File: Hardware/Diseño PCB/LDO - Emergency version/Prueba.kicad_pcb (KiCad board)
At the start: 2 copper layers, 99.4 x 209.5 mm, 132 parts, among them Q1 BC547, Q10 BC547, Q11 BC557, Q12 BC547, Q13 BC557, Q14 BC547, Q15 BC557, Q16 BC547, Q17 BC547, Q18 BC557, Q19 IRF4905, Q2 BC547, Q3 BC557, Q39 BC547, Q4 BC547, Q40 BC547, Q41 BC557, Q42 BC547, Q43 BC557, Q44 BC547, Q45 BC547, Q46 BC547, Q47 BC557, Q48 BC547, Q49 BC557, Q5 BC557, Q50 BC547, Q51 BC557, Q52 BC547, Q53 BC557, Q54 BC547, Q55 BC547, Q56 BC557, Q57 IRF4905, Q6 BC547, Q7 BC547, Q8 BC547, Q9 BC557, U1 LM324, U2 TL431LP, U5 LM324, U6 TL431LP

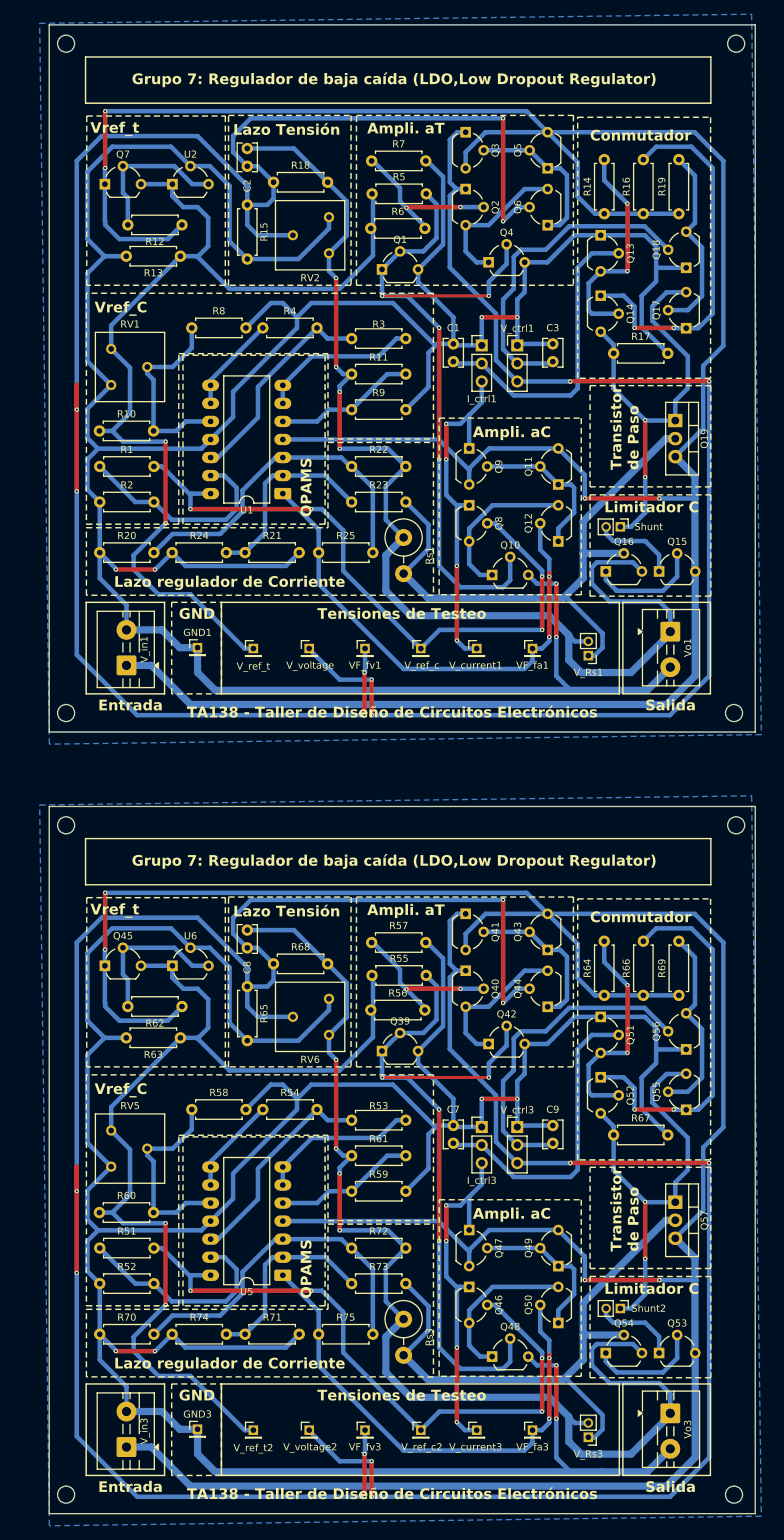
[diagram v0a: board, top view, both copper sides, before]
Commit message: Correcciones menores en emergency version
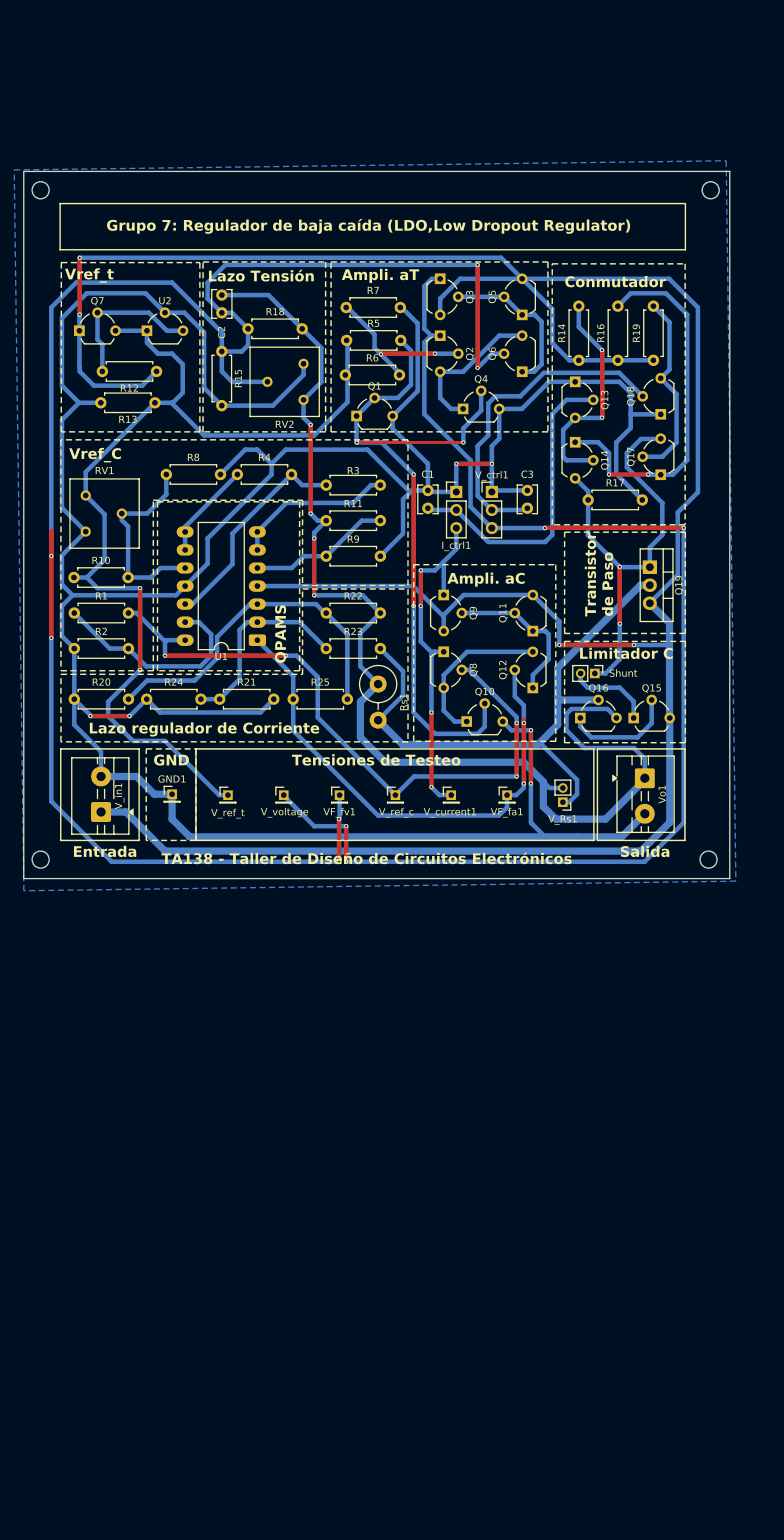
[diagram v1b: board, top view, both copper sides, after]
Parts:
- removed C7: 220 nF, Capacitor_THT:C_Disc_D3.8mm_W2.6mm_P2.50mm
- removed C8: 100pF, Capacitor_THT:C_Disc_D3.8mm_W2.6mm_P2.50mm
- removed C9: 2.2nF, Capacitor_THT:C_Disc_D3.8mm_W2.6mm_P2.50mm
- removed G***2: LOGO, LOGO
- removed GND3: Pin_GND, Connector_PinHeader_2.00mm:PinHeader_1x01_P2.00mm_Vertical
- removed I_ctrl3: I_ctrl, Connector_PinHeader_2.54mm:PinHeader_1x03_P2.54mm_Vertical
- removed Q39, Q40, Q42, Q44, Q45, Q46, Q48, Q50, Q52, Q54, Q55: BC547, Package_TO_SOT_THT:TO-92_Wide
- removed Q41, Q43, Q47, Q49, Q51, Q53, Q56: BC557, Package_TO_SOT_THT:TO-92_Wide
- removed Q57: IRF4905, Package_TO_SOT_THT:TO-220-3_Vertical
- removed R51, R52, R53, R54, R55, R59, R65, R66, R72, R73: 1k, Resistor_THT:R_Axial_DIN0207_L6.3mm_D2.5mm_P7.62mm_Horizontal
- removed R56, R57, R62: 2.2k, Resistor_THT:R_Axial_DIN0207_L6.3mm_D2.5mm_P7.62mm_Horizontal
- removed R58: 910, Resistor_THT:R_Axial_DIN0207_L6.3mm_D2.5mm_P7.62mm_Horizontal
- removed R60, R68: 3k3, Resistor_THT:R_Axial_DIN0207_L6.3mm_D2.5mm_P7.62mm_Horizontal
- removed R61: 2k2, Resistor_THT:R_Axial_DIN0207_L6.3mm_D2.5mm_P7.62mm_Horizontal
- removed R63, R64, R67, R69, R71, R75: 10k, Resistor_THT:R_Axial_DIN0207_L6.3mm_D2.5mm_P7.62mm_Horizontal
- removed R70, R74: 4.7k, Resistor_THT:R_Axial_DIN0207_L6.3mm_D2.5mm_P7.62mm_Horizontal
- removed RV5, RV6: Preset, Potentiometer_THT:Potentiometer_Bourns_3386F_Vertical
- removed Rs3: 0.2, Resistor_THT:R_Axial_DIN0516_L15.5mm_D5.0mm_P5.08mm_Vertical
- removed Shunt2: Shunt, Connector_PinHeader_2.00mm:PinHeader_1x02_P2.00mm_Vertical
- removed U5: LM324, Package_DIP:DIP-14_W10.16mm_LongPads
- removed U6: TL431LP, Package_TO_SOT_THT:TO-92_Wide
- removed VF_fa3: VF_fa, Connector_PinHeader_2.00mm:PinHeader_1x01_P2.00mm_Vertical
- removed VF_fv3: VF_fv, Connector_PinHeader_2.00mm:PinHeader_1x01_P2.00mm_Vertical
- removed V_Rs3: V_Rs, Connector_PinHeader_2.00mm:PinHeader_1x02_P2.00mm_Vertical
- removed V_ctrl3: V_ctrl, Connector_PinHeader_2.54mm:PinHeader_1x03_P2.54mm_Vertical
- removed V_current3: V_current, Connector_PinHeader_2.00mm:PinHeader_1x01_P2.00mm_Vertical
- removed V_in3: Vin, TerminalBlock:TerminalBlock_MaiXu_MX126-5.0-02P_1x02_P5.00mm
- removed V_ref_c2: V_ref_c_test, Connector_PinHeader_2.00mm:PinHeader_1x01_P2.00mm_Vertical
- removed V_ref_t2: V_ref_test, Connector_PinHeader_2.00mm:PinHeader_1x01_P2.00mm_Vertical
- removed V_voltage2: V_voltage_test, Connector_PinHeader_2.00mm:PinHeader_1x01_P2.00mm_Vertical
- removed Vo3: Vo, TerminalBlock:TerminalBlock_MaiXu_MX126-5.0-02P_1x02_P5.00mm
- moved Q15 20.9 mm to (135.7, 135.4)
- moved Q16 20.9 mm to (128.2, 135.4)
- moved I_ctrl1 20.9 mm to (110.8, 103.6)
- moved Q10 20.9 mm to (112.2, 135.9)
- moved Q13 20.9 mm to (127.5, 88.1)
- moved Q14 20.9 mm to (127.5, 96.6)
- moved Q8 20.9 mm to (109.0, 126.1)
- moved Q9 20.9 mm to (109.0, 118.1)
- moved V_ctrl1 20.9 mm to (115.8, 103.6)
- moved Q2 20.9 mm to (108.5, 81.6)
- moved Q3 20.9 mm to (108.5, 73.6)
- moved Q5 20.9 mm to (120.0, 78.7)
- moved Q17 20.9 mm to (139.5, 101.2)
- moved Q18 20.9 mm to (139.5, 92.7)
- moved R17 20.9 mm to (129.3, 104.7)
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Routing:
- net GND: track 906.1 -> 453.1 mm, vias 12 -> 6
- net Vcc: track 775.3 -> 387.7 mm, vias 8 -> 4
- net VF_fv: track 489.9 -> 245.0 mm, vias 12 -> 6
- net V_voltage: track 353.4 -> 176.7 mm, vias 8 -> 4
- net -V_Rs: track 334.5 -> 167.2 mm, vias 8 -> 4
- net Vref: track 280.5 -> 140.2 mm, vias 4 -> 2
- net nodo A: track 203.3 -> 101.7 mm, vias 8 -> 4
- net Vref_c: track 185.2 -> 92.6 mm, vias 8 -> 4
- net +V_Rs: track 175.5 -> 87.7 mm
- net VF_fa: track 145.7 -> 72.8 mm, vias 4 -> 2
- net Vctrl: track 123.2 -> 61.6 mm, vias 4 -> 2
- net Net-(Q14-C): track 105.1 -> 52.5 mm, vias 4 -> 2
- net V_current: track 100.5 -> 50.2 mm, vias 8 -> 4
- net Net-(U1A-+): track 98.0 -> 49.0 mm
- net Net-(Q18-B): track 92.9 -> 46.4 mm
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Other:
- board size 99.4 x 209.5 mm -> 99.4 x 99.5 mm

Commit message: Cambios menores a informe y actualización de placa
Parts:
- removed V_ref_c: V_ref_c_test, Connector_PinHeader_2.00mm:PinHeader_1x01_P2.00mm_Vertical
- removed V_ref_t: V_ref_test, Connector_PinHeader_2.00mm:PinHeader_1x01_P2.00mm_Vertical
- removed V_voltage: V_voltage_test, Connector_PinHeader_2.00mm:PinHeader_1x01_P2.00mm_Vertical
- added C1: 10uF, Capacitor_THT:C_Radial_D5.0mm_H11.0mm_P2.00mm, F.Cu at (69.5, 143.0)
- added V_ref_c1: V_ref_c, Connector_PinHeader_2.00mm:PinHeader_1x01_P2.00mm_Vertical, F.Cu at (102.5, 146.5)
- added V_ref_t1: V_ref_t, Connector_PinHeader_2.00mm:PinHeader_1x01_P2.00mm_Vertical, F.Cu at (78.5, 146.5)
- added V_voltage1: V_voltage, Connector_PinHeader_2.00mm:PinHeader_1x01_P2.00mm_Vertical, F.Cu at (86.5, 146.5)
- RV1, RV2: footprint Potentiometer_THT:Potentiometer_Bourns_3386F_Vertical -> Potentiometer_THT:Potentiometer_Bourns_3386P_Vertical
- moved GND1 3.88 mm to (70.5, 150.0)
- moved RV2 3.03 mm to (86.2, 85.5)
- moved RV1 2.54 mm to (61.1, 109.2)
- moved Vo1 0.37 mm to (137.3, 144.2)
- moved VF_fa1 0.25 mm to (117.9, 146.5)
- moved VF_fv1 0.25 mm to (94.3, 146.5)
- moved V_current1 0.25 mm to (110.0, 146.5)
- renumbered C1 to C2, C2 to C3, C3 to C4, Shunt to J1
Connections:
- R20 pad 2: Net-(U1A-+) -> Net-(U1A--)
- R21 pad 1: Net-(U1A--) -> Net-(U1A-+)
- R22 pad 1: Net-(U1A-+) -> Net-(U1A--)
- R23 pad 1: Net-(U1A--) -> Net-(U1A-+)
- R24 pad 2: Net-(U1A--) -> Net-(U1A-+)
- R25 pad 2: Net-(U1A-+) -> Net-(U1A--)
- V_in1 pad 1: Vcc -> GND
- V_in1 pad 2: GND -> Vcc
- Vo1 pad 1: GND -> -V_Rs
- Vo1 pad 2: -V_Rs -> GND
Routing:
- net Net-(U1A--): track 27.7 -> 65.2 mm
- net Vcc: track 387.7 -> 408.5 mm
- net Net-(U1A-+): track 49.0 -> 31.5 mm
- net -V_Rs: track 167.2 -> 179.9 mm
- net GND: track 453.1 -> 462.8 mm
- net VF_fv: track 245.0 -> 246.5 mm
- net +V_Rs: track 87.7 -> 88.8 mm
- net Vref: track 140.2 -> 139.6 mm
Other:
- board text removed: "GND"

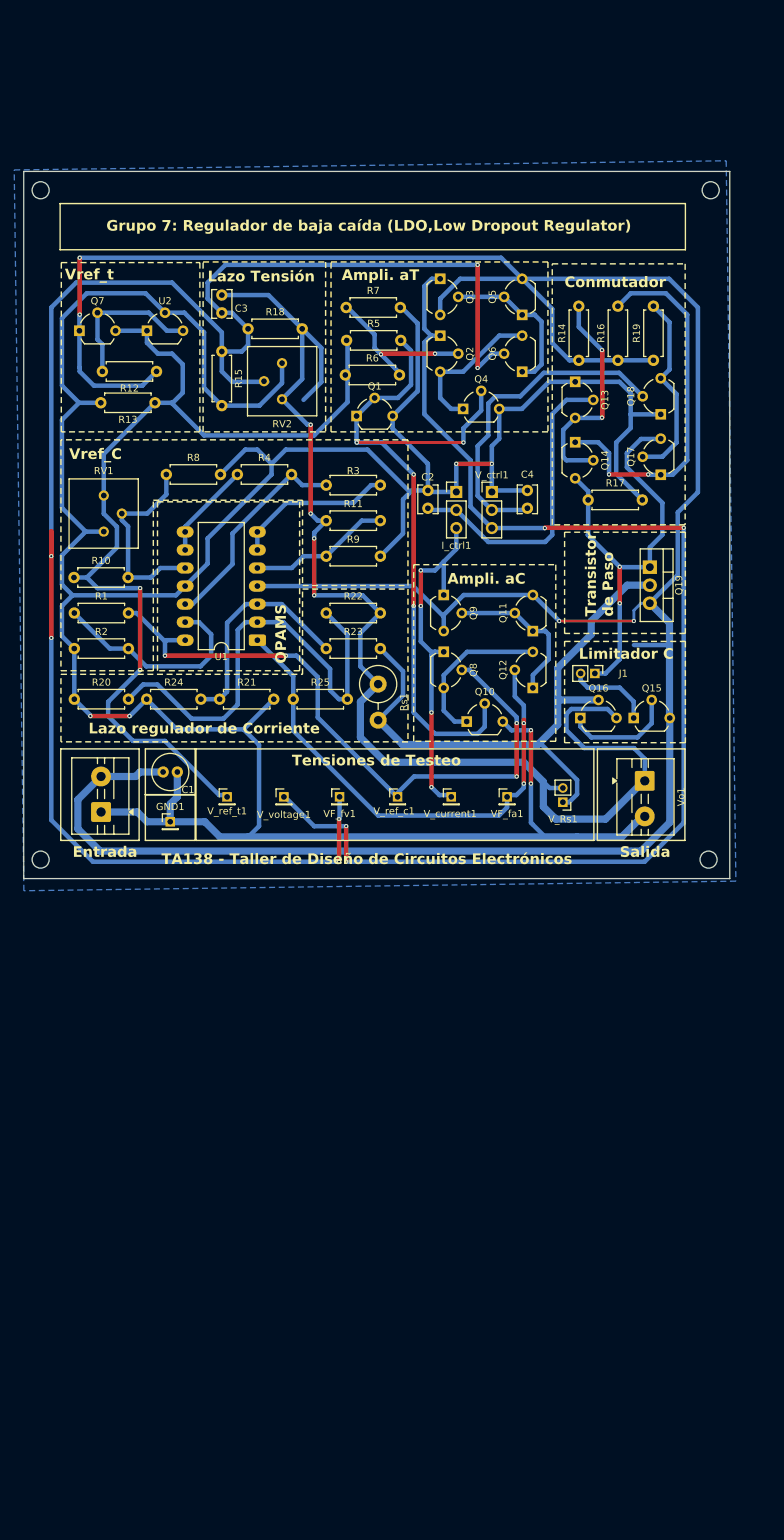
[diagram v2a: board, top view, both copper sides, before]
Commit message: Cambios al informe CHK3
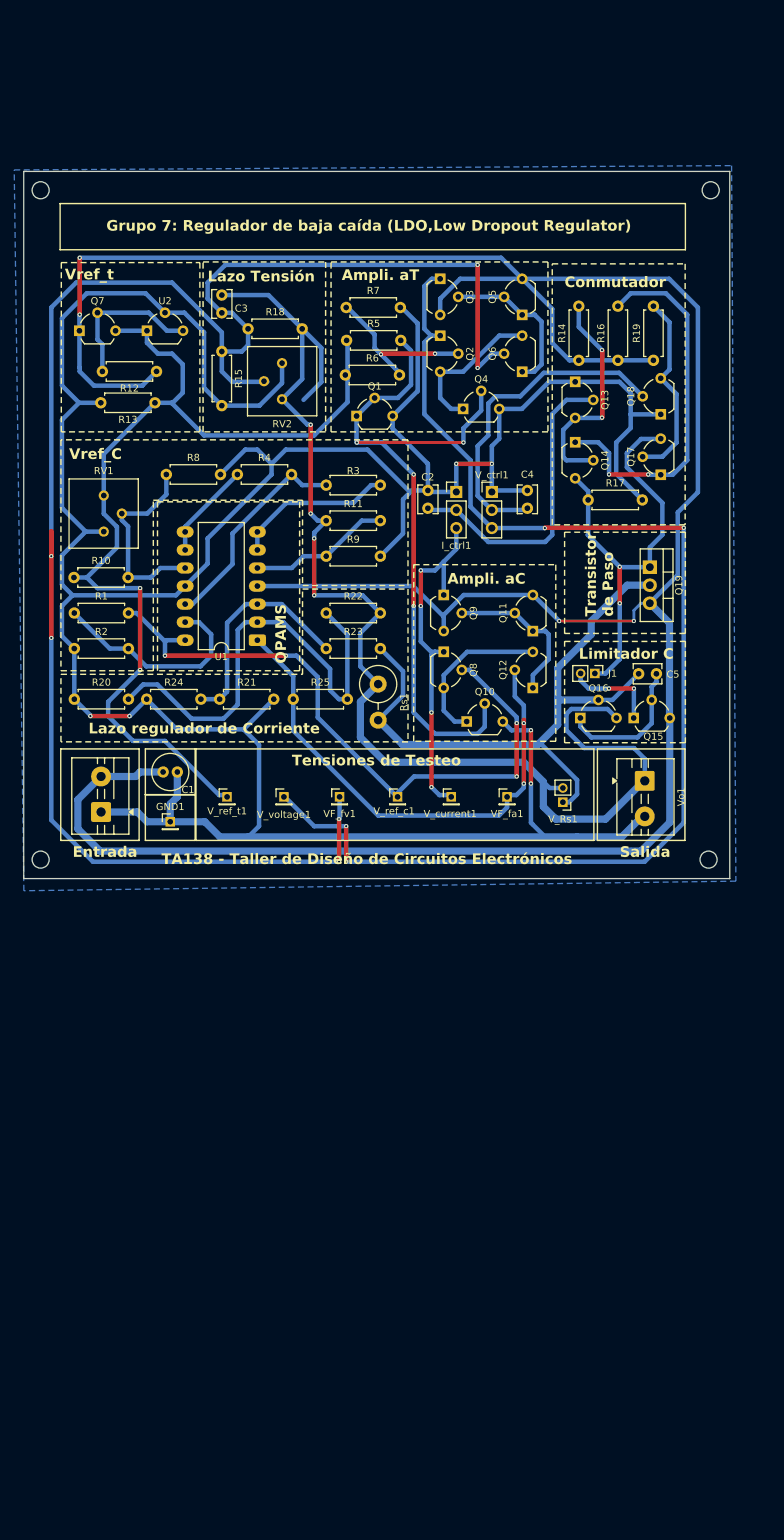
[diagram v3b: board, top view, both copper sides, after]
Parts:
- added C5: 220 nF, Capacitor_THT:C_Disc_D3.8mm_W2.6mm_P2.50mm, F.Cu at (138.9, 129.2)
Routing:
- net +V_Rs: track 88.8 -> 96.0 mm
- net Vcc: track 408.5 -> 403.5 mm
- net Net-(Q15-B): track 16.0 -> 19.9 mm
- net Net-(J1-Pin_2): track 12.0 -> 13.1 mm, vias 0 -> 2
